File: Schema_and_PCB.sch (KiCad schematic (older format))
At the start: 7 parts, among them SW1 PST-11A, U6 STM32H743ZIT6

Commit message: Buttons complete
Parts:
- removed U6: STM32H743ZIT6, QFP50P2200X2200X160-144N, symbol SVIELCOM_Library:STM32H743ZIT6
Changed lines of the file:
@@
 $Descr A3 16535 11693
 encoding utf-8
-Sheet 1 9
+Sheet 1 10
 Title "ШВУ"
 Date "2021-03-25"
@@
 F1 "Indicator.sch" 50
 $EndSheet
-$Comp
-L SVIELCOM_Library:STM32H743ZIT6 U6
-U 2 1 6096B351
-P 8030 7680
-F 0 "U6" H 8080 9347 50  0000 C CNN
-F 1 "STM32H743ZIT6" H 8080 9256 50  0000 C CNN
-F 2 "QFP50P2200X2200X160-144N" H 8080 9280 50  0001 L BNN
-F 3 "" H 8080 9680 50  0001 L BNN
-F 4 "STMicroelectronics" H 8080 9380 50  0001 L BNN "MANUFACTURER"
-F 5 "7" H 8080 9680 50  0001 L BNN "PARTREV"
-F 6 "1.6 mm" H 8080 9580 50  0001 L BNN "MAXIMUM_PACKAGE_HEIGHT"
-F 7 "IPC-7351B" H 8080 9480 50  0001 L BNN "STANDARD"
-	2    8030 7680
-	1    0    0    -1
-$EndComp
 $Sheet
 S 2610 6310 1270 900

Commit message: begin MCU editing
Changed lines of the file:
@@
 $Descr A3 16535 11693
 encoding utf-8
-Sheet 1 10
+Sheet 1 9
 Title "ШВУ"
 Date "2021-03-25"
@@
 $EndSheet
 $Sheet
-S 3010 9870 1380 950
-U 60CDBB10
-F0 "Main_power" 50
-F1 "Main_power.sch" 50
-$EndSheet
-$Sheet
-S 5030 9870 1290 950
+S 2920 9860 1290 950
 U 60CDBD15
 F0 "Buttons" 50

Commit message: Probably pre-alpha version is done
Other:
- moved on the sheet: C1, C2, C3, C4, C5, SW1A
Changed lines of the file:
@@
 L Device:C C4
 U 1 1 606157F0
-P 5090 -1500
-F 0 "C4" H 5205 -1454 50  0000 L CNN
-F 1 "1µF" H 5205 -1545 50  0000 L CNN
-F 2 "Capacitor_SMD:C_0603_1608Metric_Pad1.08x0.95mm_HandSolder" H 5128 -1650 50  0001 C CNN
-F 3 "http://www.farnell.com/datasheets/2710676.pdf" H 5090 -1500 50  0001 C CNN
-F 4 "CL10B105KA8NNNC" H 5090 -1500 50  0001 C CNN "Type"
-	1    5090 -1500
+P -860 10780
+F 0 "C4" H -745 10826 50  0000 L CNN
+F 1 "1µF" H -745 10735 50  0000 L CNN
+F 2 "Capacitor_SMD:C_0603_1608Metric_Pad1.08x0.95mm_HandSolder" H -822 10630 50  0001 C CNN
+F 3 "http://www.farnell.com/datasheets/2710676.pdf" H -860 10780 50  0001 C CNN
+F 4 "CL10B105KA8NNNC" H -860 10780 50  0001 C CNN "Type"
+	1    -860 10780
 	1    0    0    -1
 $EndComp
@@
 L Device:CP C3
 U 1 1 6061539B
-P 5350 -1880
-F 0 "C3" H 5468 -1834 50  0000 L CNN
-F 1 "10µF" H 5468 -1925 50  0000 L CNN
-F 2 "Capacitor_Tantalum_SMD:CP_EIA-3216-10_Kemet-I" H 5388 -2030 50  0001 C CNN
-F 3 "http://www.mouser.com/ds/2/427/593d-239975.pdf" H 5350 -1880 50  0001 C CNN
-F 4 "593D106X9016A2TE3" H 5350 -1880 50  0001 C CNN "Type"
-	1    5350 -1880
+P -880 10170
+F 0 "C3" H -762 10216 50  0000 L CNN
+F 1 "10µF" H -762 10125 50  0000 L CNN
+F 2 "Capacitor_Tantalum_SMD:CP_EIA-3216-10_Kemet-I" H -842 10020 50  0001 C CNN
+F 3 "http://www.mouser.com/ds/2/427/593d-239975.pdf" H -880 10170 50  0001 C CNN
+F 4 "593D106X9016A2TE3" H -880 10170 50  0001 C CNN "Type"
+	1    -880 10170
 	1    0    0    -1
 $EndComp
@@
 L Device:CP C2
 U 1 1 6061A793
-P 5910 -1910
-F 0 "C2" H 6028 -1864 50  0000 L CNN
-F 1 "47µFx25" H 6028 -1955 50  0000 L CNN
-F 2 "Capacitor_Tantalum_SMD:CP_EIA-6032-28_Kemet-C_Pad2.25x2.35mm_HandSolder" H 5948 -2060 50  0001 C CNN
-F 3 "https://www.farnell.com/datasheets/1878216.pdf" H 5910 -1910 50  0001 C CNN
-F 4 "TR3D476K025C0150" H 5910 -1910 50  0001 C CNN "Type"
-	1    5910 -1910
+P -870 9540
+F 0 "C2" H -752 9586 50  0000 L CNN
+F 1 "47µFx25" H -752 9495 50  0000 L CNN
+F 2 "Capacitor_Tantalum_SMD:CP_EIA-6032-28_Kemet-C_Pad2.25x2.35mm_HandSolder" H -832 9390 50  0001 C CNN
+F 3 "https://www.farnell.com/datasheets/1878216.pdf" H -870 9540 50  0001 C CNN
+F 4 "TR3D476K025C0150" H -870 9540 50  0001 C CNN "Type"
+	1    -870 9540
 	1    0    0    -1
 $EndComp
@@
 L Device:C C1
 U 1 1 60633F0C
-P 4360 -2450
-F 0 "C1" H 4475 -2404 50  0000 L CNN
-F 1 "1µF" H 4475 -2495 50  0000 L CNN
-F 2 "Capacitor_SMD:C_0603_1608Metric_Pad1.08x0.95mm_HandSolder" H 4398 -2600 50  0001 C CNN
-F 3 "https://www.farnell.com/datasheets/2048520.pdf" H 4360 -2450 50  0001 C CNN
-F 4 "GRM188R7YA105KA12D" H 4360 -2450 50  0001 C CNN "Type"
-	1    4360 -2450
+P -970 8930
+F 0 "C1" H -855 8976 50  0000 L CNN
+F 1 "1µF" H -855 8885 50  0000 L CNN
+F 2 "Capacitor_SMD:C_0603_1608Metric_Pad1.08x0.95mm_HandSolder" H -932 8780 50  0001 C CNN
+F 3 "https://www.farnell.com/datasheets/2048520.pdf" H -970 8930 50  0001 C CNN
+F 4 "GRM188R7YA105KA12D" H -970 8930 50  0001 C CNN "Type"
+	1    -970 8930
 	1    0    0    -1
 $EndComp
@@
 L Device:CP C5
 U 1 1 60634752
-P 6480 -1480
-F 0 "C5" H 6598 -1434 50  0000 L CNN
-F 1 "47µFx16" H 6598 -1525 50  0000 L CNN
-F 2 "Capacitor_Tantalum_SMD:CP_EIA-7343-31_Kemet-D_Pad2.25x2.55mm_HandSolder" H 6518 -1630 50  0001 C CNN
-F 3 "https://www.farnell.com/datasheets/1995953.pdf" H 6480 -1480 50  0001 C CNN
-F 4 "593D476X9016D2TE3" H 6480 -1480 50  0001 C CNN "Type"
-	1    6480 -1480
+P -940 8310
+F 0 "C5" H -822 8356 50  0000 L CNN
+F 1 "47µFx16" H -822 8265 50  0000 L CNN
+F 2 "Capacitor_Tantalum_SMD:CP_EIA-7343-31_Kemet-D_Pad2.25x2.55mm_HandSolder" H -902 8160 50  0001 C CNN
+F 3 "https://www.farnell.com/datasheets/1995953.pdf" H -940 8310 50  0001 C CNN
+F 4 "593D476X9016D2TE3" H -940 8310 50  0001 C CNN "Type"
+	1    -940 8310
 	1    0    0    -1
 $EndComp
@@
 L Switch:SW_DPDT_x2 SW1
 U 1 1 6063E7A3
-P 8930 -2060
-F 0 "SW1" H 8930 -1775 50  0000 C CNN
-F 1 "PST-11A" H 8930 -1866 50  0000 C CNN
-F 2 "" H 8930 -2060 50  0001 C CNN
-F 3 "https://www.terraelectronica.ru/product/45953" H 8930 -2060 50  0001 C CNN
-	1    8930 -2060
+P -830 7470
+F 0 "SW1" H -830 7755 50  0000 C CNN
+F 1 "PST-11A" H -830 7664 50  0000 C CNN
+F 2 "" H -830 7470 50  0001 C CNN
+F 3 "https://www.terraelectronica.ru/product/45953" H -830 7470 50  0001 C CNN
+	1    -830 7470
 	1    0    0    -1
 $EndComp

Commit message: v0.1
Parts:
- renumbered C5 to C1, C1 to C2, C2 to C3, C3 to C4, C4 to C5
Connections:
- no-connect marks 0 -> 13
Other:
- moved on the sheet: C1, C2, C3, C4, C5, SW1A

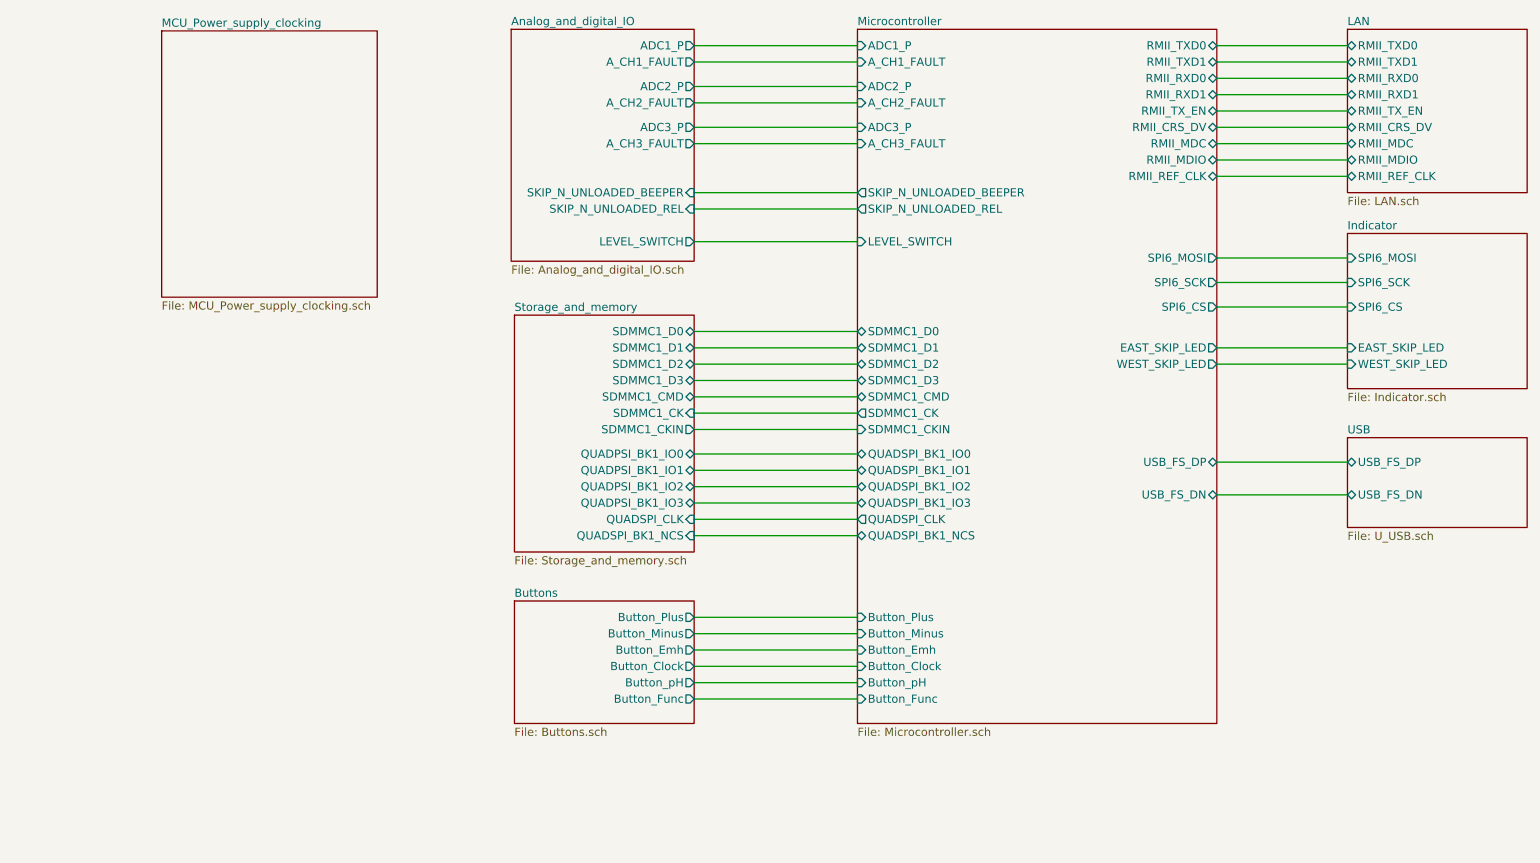
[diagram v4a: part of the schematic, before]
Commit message: v0.2 added ecoder inputs
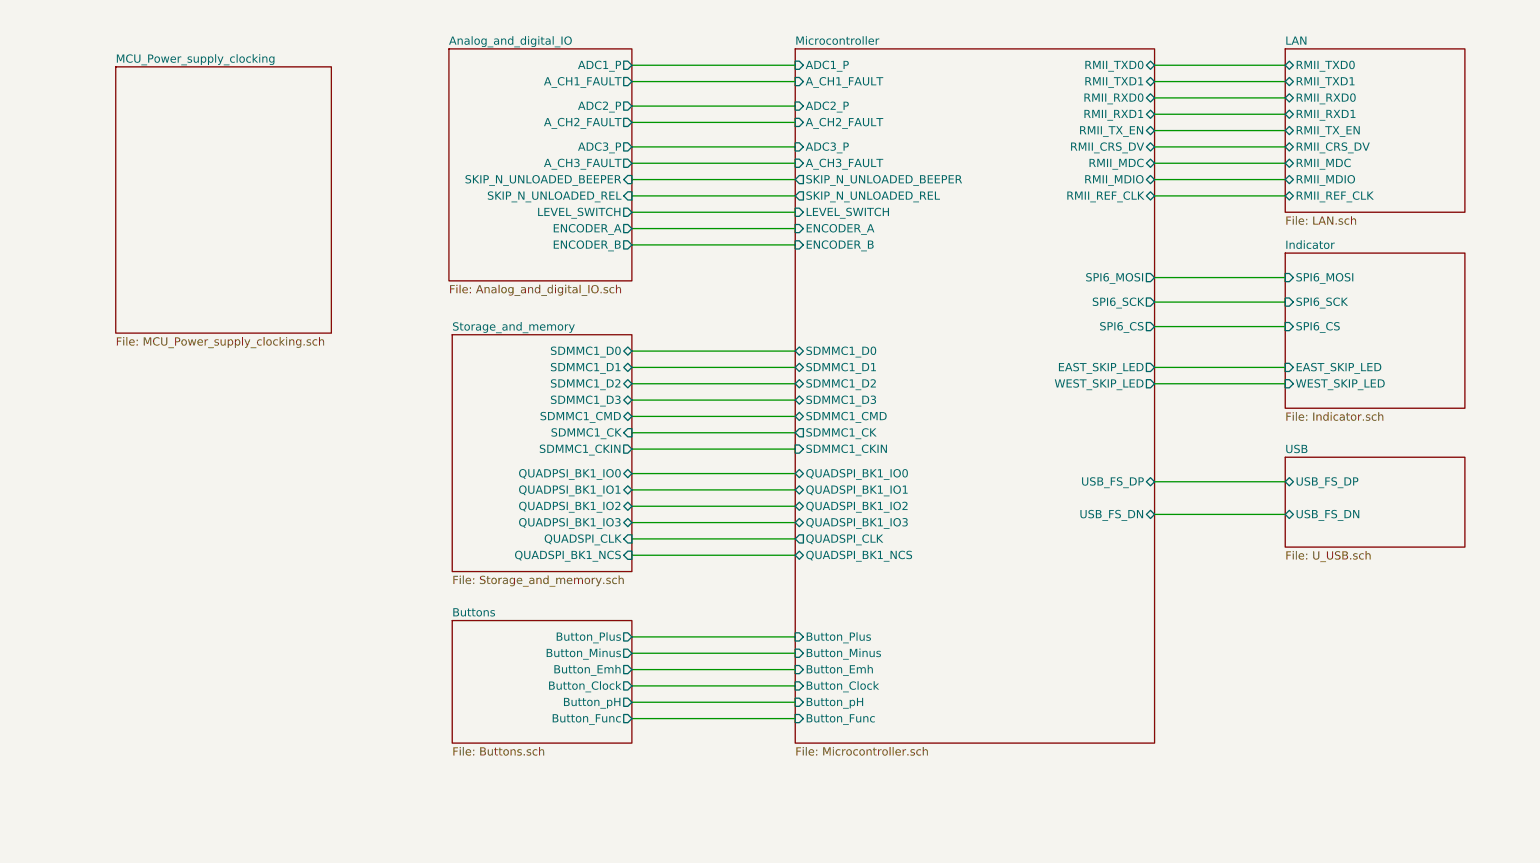
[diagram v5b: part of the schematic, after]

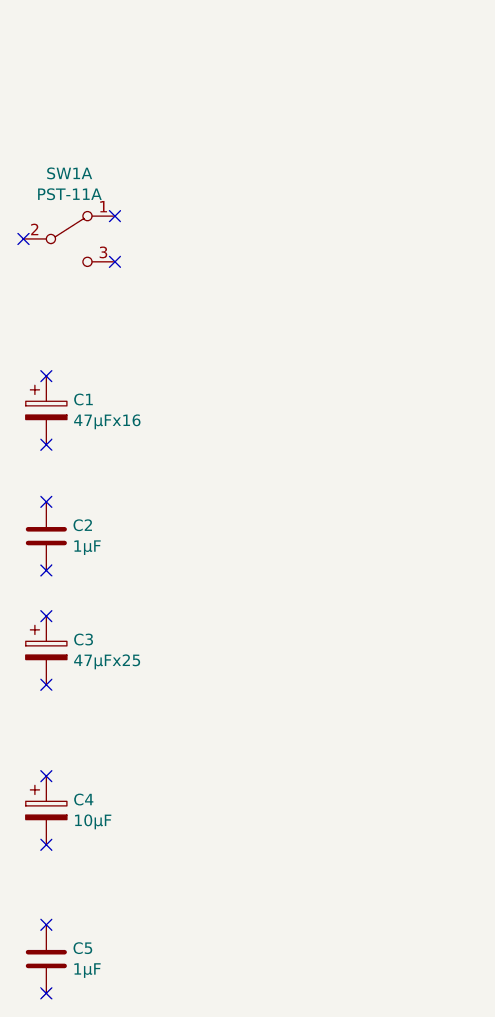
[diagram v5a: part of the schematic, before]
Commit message: v0.3 changed sd_card holder
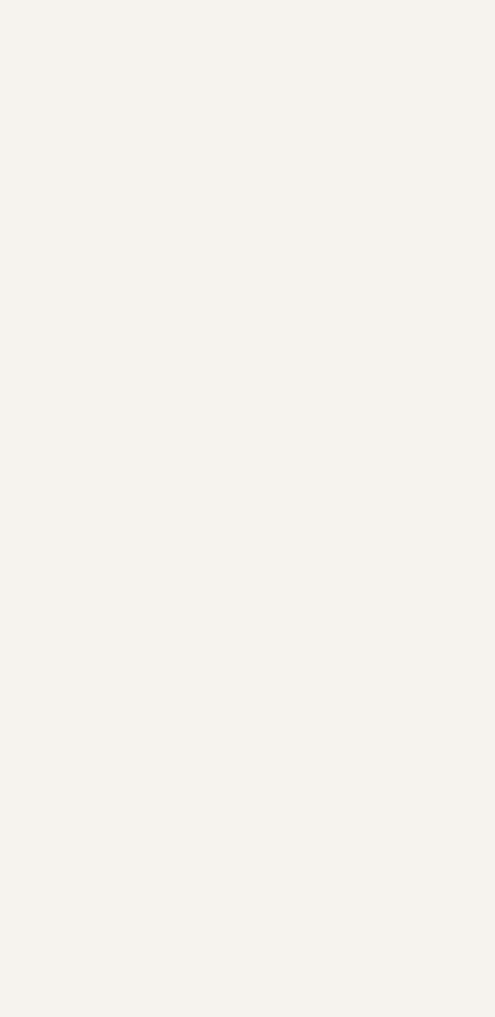
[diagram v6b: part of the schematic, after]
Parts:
- removed C1: 47µFx16, Capacitor_Tantalum_SMD:CP_EIA-7343-31_Kemet-D_Pad2.25x2.55mm_HandSolder, symbol Device:CP
- removed C2, C5: 1µF, Capacitor_SMD:C_0603_1608Metric_Pad1.08x0.95mm_HandSolder, symbol Device:C
- removed C3: 47µFx25, Capacitor_Tantalum_SMD:CP_EIA-6032-28_Kemet-C_Pad2.25x2.35mm_HandSolder, symbol Device:CP
- removed C4: 10µF, Capacitor_Tantalum_SMD:CP_EIA-3216-10_Kemet-I, symbol Device:CP
- removed SW1: PST-11A, symbol Switch:SW_DPDT_x2
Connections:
- no-connect marks 13 -> 0
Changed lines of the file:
@@
 Comment4 ""
 $EndDescr
-$Comp
-L Device:C C5
-U 1 1 606157F0
-P -580 6480
-F 0 "C5" H -465 6526 50  0000 L CNN
-F 1 "1µF" H -465 6435 50  0000 L CNN
-F 2 "Capacitor_SMD:C_0603_1608Metric_Pad1.08x0.95mm_HandSolder" H -542 6330 50  0001 C CNN
-F 3 "http://www.farnell.com/datasheets/2710676.pdf" H -580 6480 50  0001 C CNN
-F 4 "CL10B105KA8NNNC" H -580 6480 50  0001 C CNN "Type"
-	1    -580 6480
-	1    0    0    -1
-$EndComp
-$Comp
-L Device:CP C4
-U 1 1 6061539B
-P -580 5830
-F 0 "C4" H -462 5876 50  0000 L CNN
-F 1 "10µF" H -462 5785 50  0000 L CNN
-F 2 "Capacitor_Tantalum_SMD:CP_EIA-3216-10_Kemet-I" H -542 5680 50  0001 C CNN
-F 3 "http://www.mouser.com/ds/2/427/593d-239975.pdf" H -580 5830 50  0001 C CNN
-F 4 "593D106X9016A2TE3" H -580 5830 50  0001 C CNN "Type"
-	1    -580 5830
-	1    0    0    -1
-$EndComp
-$Comp
-L Device:CP C3
-U 1 1 6061A793
-P -580 5130
-F 0 "C3" H -462 5176 50  0000 L CNN
-F 1 "47µFx25" H -462 5085 50  0000 L CNN
-F 2 "Capacitor_Tantalum_SMD:CP_EIA-6032-28_Kemet-C_Pad2.25x2.35mm_HandSolder" H -542 4980 50  0001 C CNN
-F 3 "https://www.farnell.com/datasheets/1878216.pdf" H -580 5130 50  0001 C CNN
-F 4 "TR3D476K025C0150" H -580 5130 50  0001 C CNN "Type"
-	1    -580 5130
-	1    0    0    -1
-$EndComp
-$Comp
-L Device:C C2
-U 1 1 60633F0C
-P -580 4630
-F 0 "C2" H -465 4676 50  0000 L CNN
-F 1 "1µF" H -465 4585 50  0000 L CNN
-F 2 "Capacitor_SMD:C_0603_1608Metric_Pad1.08x0.95mm_HandSolder" H -542 4480 50  0001 C CNN
-F 3 "https://www.farnell.com/datasheets/2048520.pdf" H -580 4630 50  0001 C CNN
-F 4 "GRM188R7YA105KA12D" H -580 4630 50  0001 C CNN "Type"
-	1    -580 4630
-	1    0    0    -1
-$EndComp
-$Comp
-L Device:CP C1
-U 1 1 60634752
-P -580 4080
-F 0 "C1" H -462 4126 50  0000 L CNN
-F 1 "47µFx16" H -462 4035 50  0000 L CNN
-F 2 "Capacitor_Tantalum_SMD:CP_EIA-7343-31_Kemet-D_Pad2.25x2.55mm_HandSolder" H -542 3930 50  0001 C CNN
-F 3 "https://www.farnell.com/datasheets/1995953.pdf" H -580 4080 50  0001 C CNN
-F 4 "593D476X9016D2TE3" H -580 4080 50  0001 C CNN "Type"
-	1    -580 4080
-	1    0    0    -1
-$EndComp
-$Comp
-L Switch:SW_DPDT_x2 SW1
-U 1 1 6063E7A3
-P -480 3330
-F 0 "SW1" H -480 3615 50  0000 C CNN
-F 1 "PST-11A" H -480 3524 50  0000 C CNN
-F 2 "" H -480 3330 50  0001 C CNN
-F 3 "https://www.terraelectronica.ru/product/45953" H -480 3330 50  0001 C CNN
-	1    -480 3330
-	1    0    0    -1
-$EndComp
 $Sheet
 S 8599 3000 1100 950
@@
 Wire Wire Line
 	4599 5850 5599 5850
-NoConn ~ -280 3430
-NoConn ~ -280 3230
-NoConn ~ -680 3330
-NoConn ~ -580 3930
-NoConn ~ -580 4230
-NoConn ~ -580 4480
-NoConn ~ -580 4780
-NoConn ~ -580 4980
-NoConn ~ -580 5280
-NoConn ~ -580 5680
-NoConn ~ -580 5980
-NoConn ~ -580 6330
-NoConn ~ -580 6630
 Wire Wire Line
 	4599 2850 5599 2850
